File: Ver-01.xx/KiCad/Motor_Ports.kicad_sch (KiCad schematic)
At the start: 28 parts

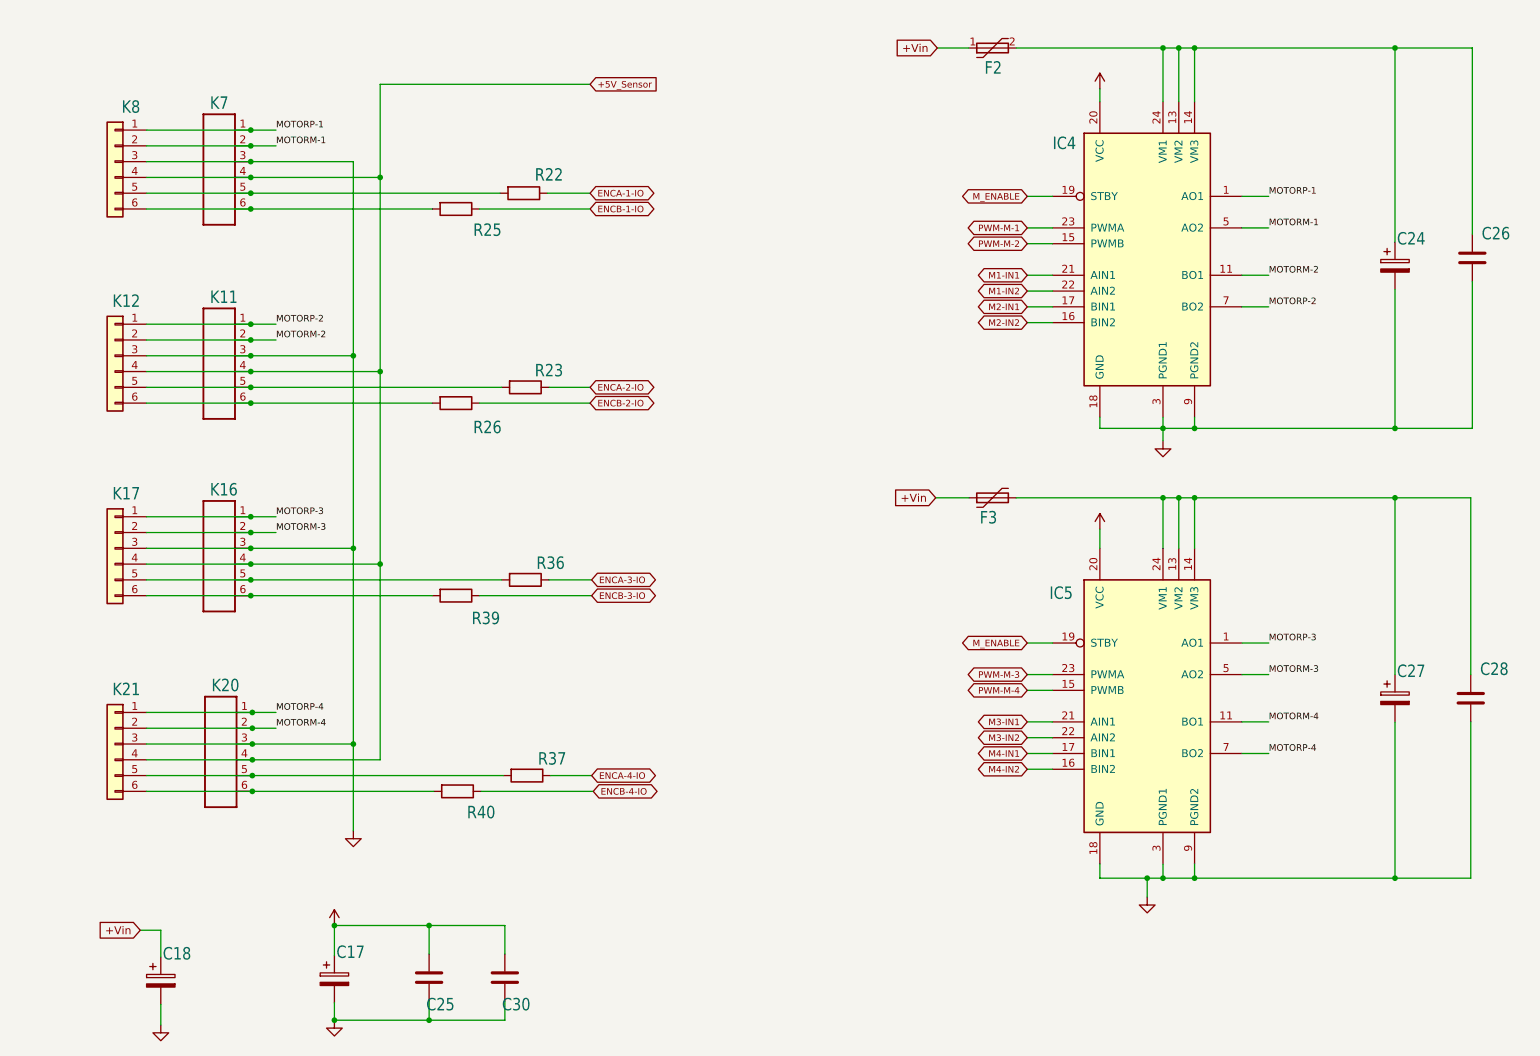
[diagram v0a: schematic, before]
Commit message: Snap to grid
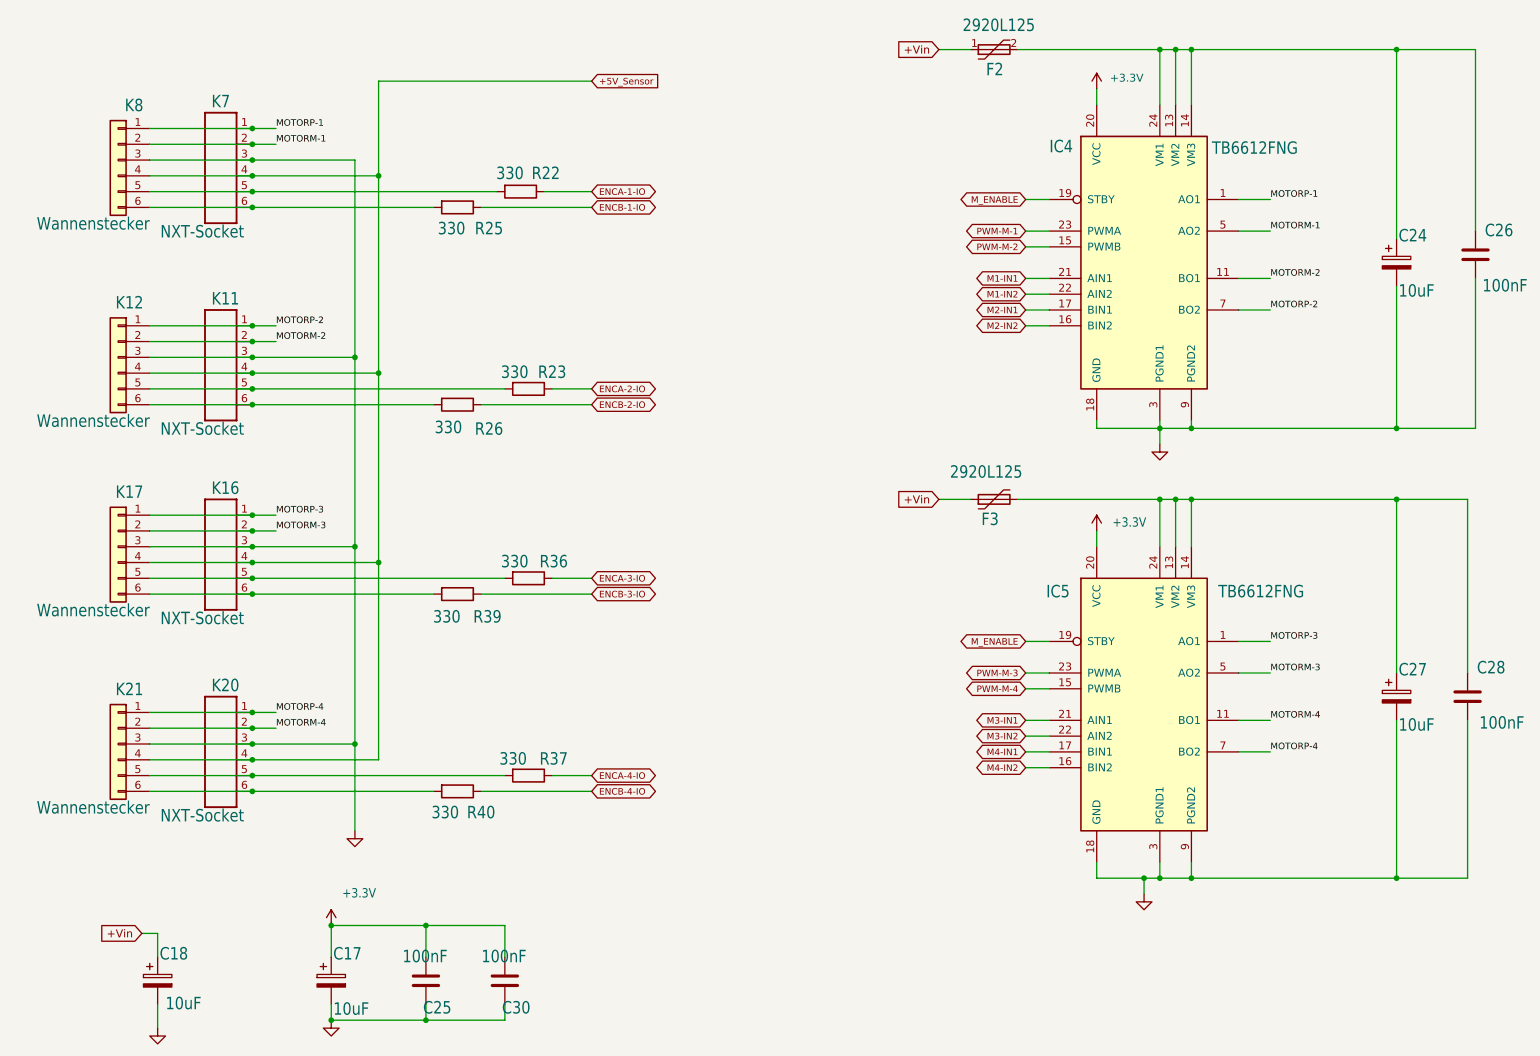
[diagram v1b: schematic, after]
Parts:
- C17, C18, C24, C27: value (none) -> 10uF; footprint (none) -> Capacitor_Tantalum_SMD:CP_EIA-3528-12_Kemet-T
- C25, C26, C28, C30: value (none) -> 100nF; footprint (none) -> Capacitor_SMD:C_0805_2012Metric
- F2, F3: value (none) -> 2920L125; footprint (none) -> Fuse:Fuse_2920_7451Metric
- IC4, IC5: value (none) -> TB6612FNG; footprint (none) -> Package_SO:SSOP-24_5.3x8.2mm_P0.65mm
- K11, K16, K20, K7: value (none) -> NXT-Socket; footprint (none) -> ORB:NXT-SOCKET
- K12, K17, K21, K8: value (none) -> Wannenstecker; footprint (none) -> ORB:IDC-Header_2x03_P2.54mm_Vertical
- R22, R23, R25, R26, R36, R37, R39, R40: value (none) -> 330; footprint (none) -> Resistor_SMD:R_0603_1608Metric
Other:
- moved on the sheet: C17, C18, C24, C25, C26, C28, C30, IC4, IC5, K12, K17, K21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
